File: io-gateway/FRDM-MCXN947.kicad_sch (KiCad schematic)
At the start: 1 part

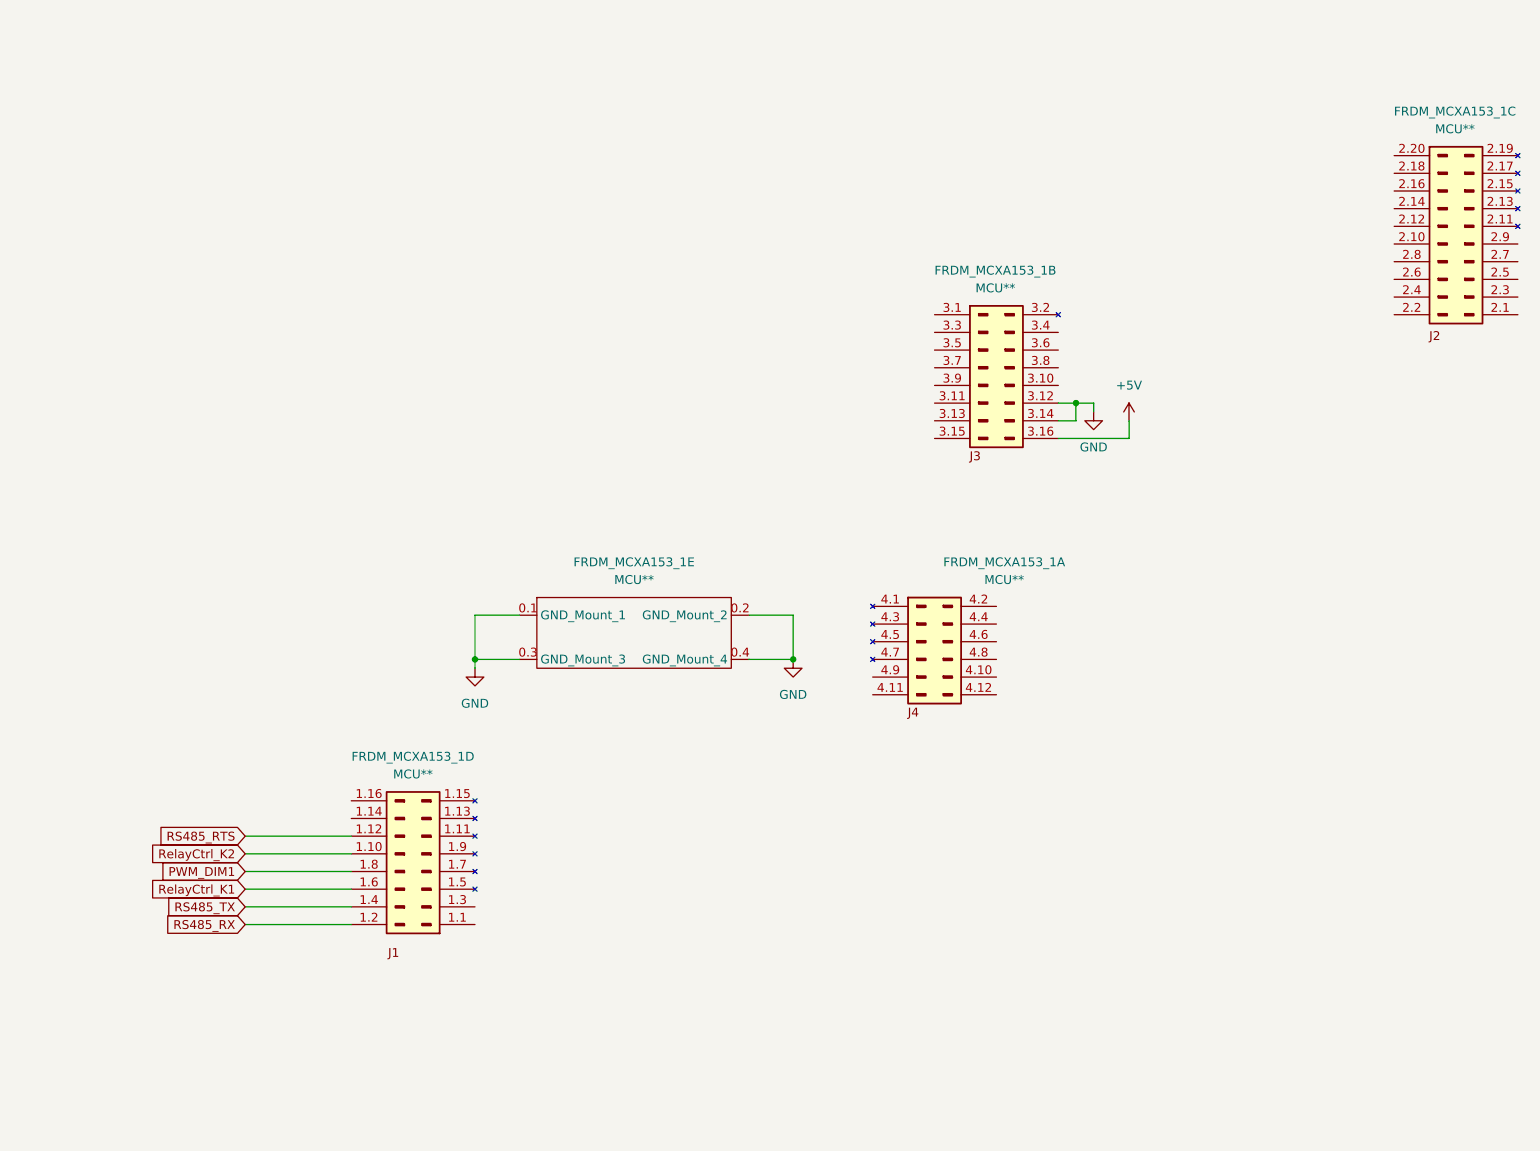
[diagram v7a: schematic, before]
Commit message: connect Relays in Schematics
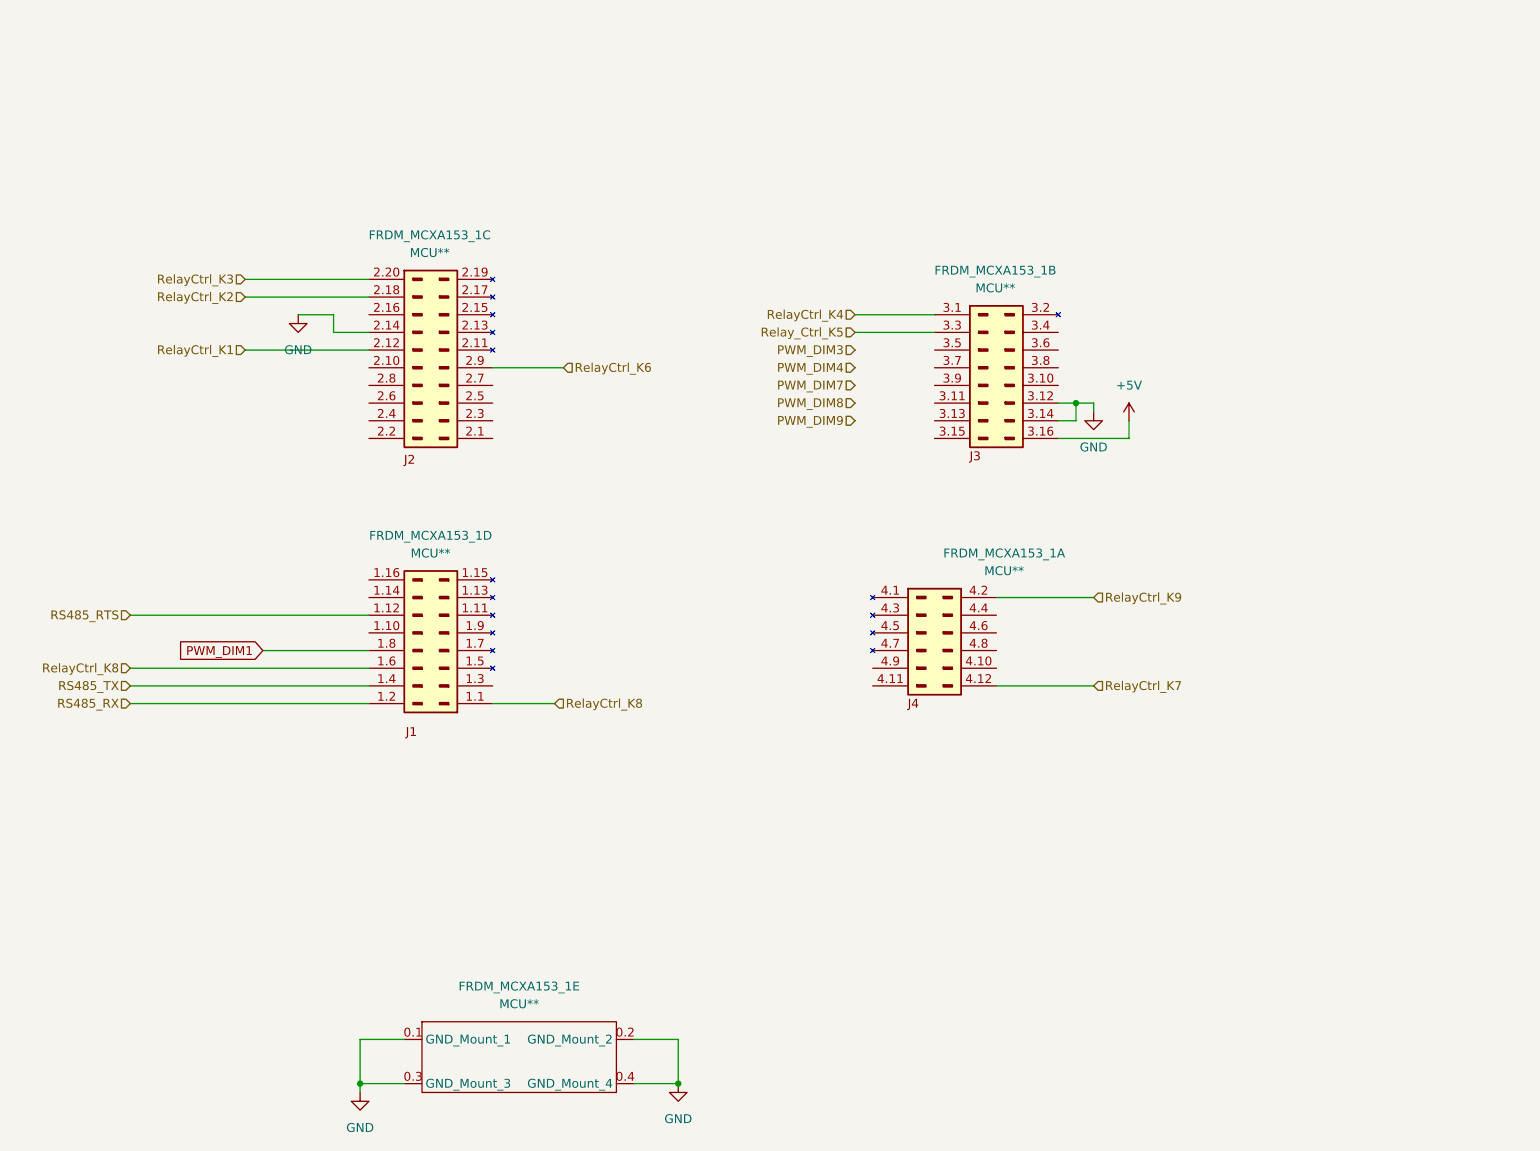
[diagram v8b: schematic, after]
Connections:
- net GND: now also FRDM_MCXA153_1.2.14 (GND)
- net RelayCtrl_K1: now also FRDM_MCXA153_1.2.12 (Pin_J2_12); no longer FRDM_MCXA153_1.1.6 (Pin_J1_6)
- net RelayCtrl_K2: now also FRDM_MCXA153_1.2.18 (Pin_J2_18); no longer FRDM_MCXA153_1.1.10 (Pin_J1_10)
- net RelayCtrl_K8: now reaches FRDM_MCXA153_1.1.1 (Pin_J1_1)
- net RelayCtrl_K8: now also FRDM_MCXA153_1.1.6 (Pin_J1_6)
- net RelayCtrl_K7: now reaches FRDM_MCXA153_1.4.12 (Pin_12)
- net RelayCtrl_K9: now reaches FRDM_MCXA153_1.4.2 (Pin_2)
- net RelayCtrl_K3: now reaches FRDM_MCXA153_1.2.20 (Pin_J2_20)
- net RelayCtrl_K6: now reaches FRDM_MCXA153_1.2.9 (Pin_J2_9)
- net RelayCtrl_K4: now reaches FRDM_MCXA153_1.3.1 (Pin_J3_1)
- net Relay_Ctrl_K5: now reaches FRDM_MCXA153_1.3.3 (Pin_J3_3)
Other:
- moved on the sheet: FRDM_MCXA153_1A, FRDM_MCXA153_1C, FRDM_MCXA153_1D, FRDM_MCXA153_1E
